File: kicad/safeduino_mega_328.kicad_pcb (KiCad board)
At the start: 2 copper layers, 134.5 x 63.9 mm, 349 parts, among them X1 USB

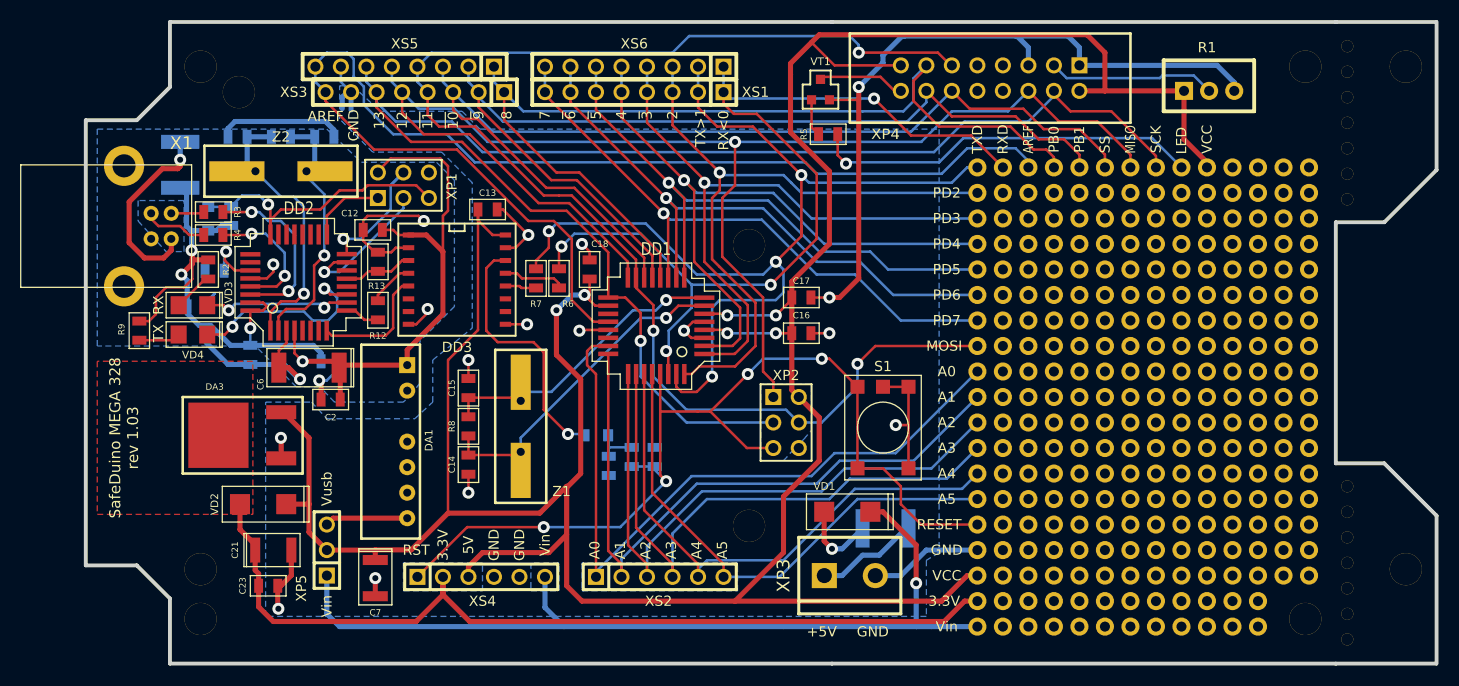
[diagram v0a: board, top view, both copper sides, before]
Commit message: Перевёл проект на Kicad 6.0.
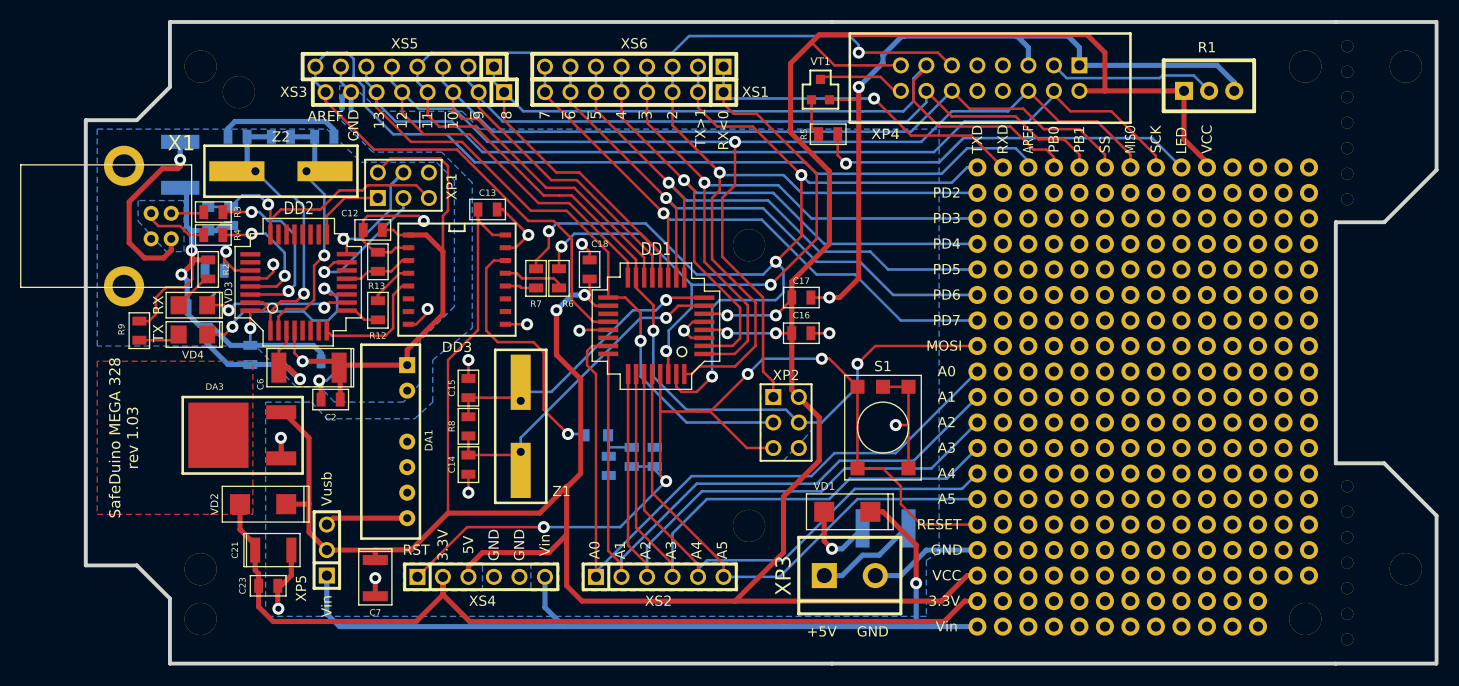
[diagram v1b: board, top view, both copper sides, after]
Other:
- net class Default removed
- board text added: "~{10}"
- board text added: "~{11}"
- board text added: "~{3}"
- board text added: "~{5}"
- board text added: "~{6}"
- board text added: "~{9}"
- board text removed: "~10"
- board text removed: "~11"
- board text removed: "~3"
- board text removed: "~5"
- board text removed: "~6"
- board text removed: "~9"
